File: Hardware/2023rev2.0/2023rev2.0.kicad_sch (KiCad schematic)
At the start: 94 parts

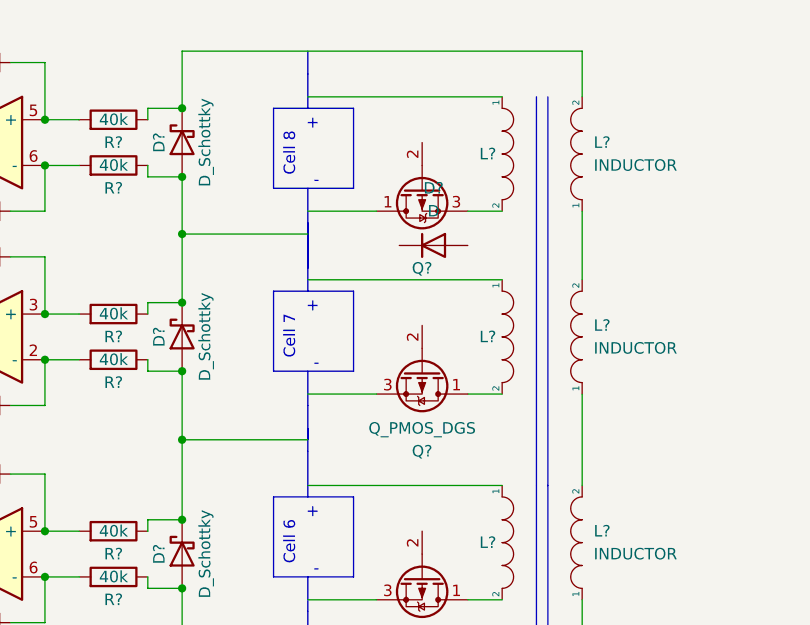
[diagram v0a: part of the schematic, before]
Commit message: Figuring out diode on secondary coils
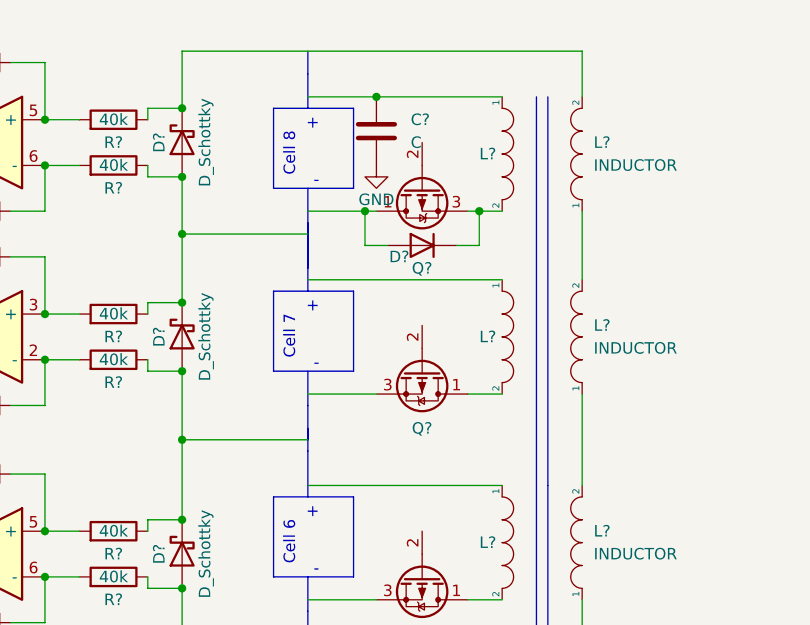
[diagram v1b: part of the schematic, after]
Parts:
- added C?: C, symbol Device:C
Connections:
- net GND: now also C?.2
- net at L?.1: now also C?.1
- net at L?.2, Q?.3 (S): now also D?.1 (K)
- net at Q?.1 (D): now also D?.2 (A)
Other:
- moved on the sheet: D?
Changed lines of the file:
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@@
   (junction (at 90.17 38.1) (diameter 0) (color 0 0 0 0)
   )
+  (junction (at 140.97 45.72) (diameter 0) (color 0 0 0 0)
+  )
   (junction (at 387.35 294.64) (diameter 0) (color 0 0 0 0)
   )
@@
   (junction (at 120.65 48.26) (diameter 0) (color 0 0 0 0)
   )
+  (junction (at 142.24 33.02) (diameter 0) (color 0 0 0 0)
+  )
   (junction (at 120.65 41.91) (diameter 0) (color 0 0 0 0)
   )
@@
   (junction (at 90.17 173.99) (diameter 0) (color 0 0 0 0)
   )
+  (junction (at 153.67 45.72) (diameter 0) (color 0 0 0 0)
+  )
   (junction (at 105.41 171.45) (diameter 0) (color 0 0 0 0)
   )
@@
     (stroke (width 0) (type default) (color 0 0 0 0))
   )
+  (wire (pts (xy 142.24 33.02) (xy 156.21 33.02))
+    (stroke (width 0) (type default) (color 0 0 0 0))
+  )
   (wire (pts (xy 386.08 294.64) (xy 387.35 294.64))
     (stroke (width 0) (type default) (color 0 0 0 0))
@@
     (stroke (width 0) (type default) (color 0 0 0 0))
   )
+  (wire (pts (xy 153.67 49.53) (xy 153.67 45.72))
+    (stroke (width 0) (type default) (color 0 0 0 0))
+  )
   (wire (pts (xy 327.66 283.21) (xy 292.1 283.21))
     (stroke (width 0) (type default) (color 0 0 0 0))
@@
     (stroke (width 0) (type default) (color 0 0 0 0))
   )
+  (wire (pts (xy 140.97 45.72) (xy 142.24 45.72))
+    (stroke (width 0) (type default) (color 0 0 0 0))
+  )
   (wire (pts (xy 87.63 186.69) (xy 93.98 186.69))
     (stroke (width 0) (type default) (color 0 0 0 0))
@@
     (stroke (width 0) (type default) (color 0 0 0 0))
   )
-  (wire (pts (xy 134.62 33.02) (xy 156.21 33.02))
+  (wire (pts (xy 134.62 33.02) (xy 142.24 33.02))
     (stroke (width 0) (type default) (color 0 0 0 0))
   )
@@
     (stroke (width 0) (type default) (color 0 0 0 0))
   )
+  (wire (pts (xy 151.13 49.53) (xy 153.67 49.53))
+    (stroke (width 0) (type default) (color 0 0 0 0))
+  )
   (wire (pts (xy 116.84 87.63) (xy 120.65 87.63))
     (stroke (width 0) (type default) (color 0 0 0 0))
   )
-  (wire (pts (xy 134.62 45.72) (xy 142.24 45.72))
+  (wire (pts (xy 134.62 45.72) (xy 140.97 45.72))
     (stroke (width 0) (type default) (color 0 0 0 0))
   )
@@
     (stroke (width 0) (type default) (color 0 0 0 0))
   )
+  (wire (pts (xy 143.51 49.53) (xy 140.97 49.53))
+    (stroke (width 0) (type default) (color 0 0 0 0))
+  )
   (wire (pts (xy 87.63 165.1) (xy 93.98 165.1))
     (stroke (width 0) (type default) (color 0 0 0 0))
@@
     (stroke (width 0) (type default) (color 0 0 0 0))
   )
+  (wire (pts (xy 153.67 45.72) (xy 156.21 45.72))
+    (stroke (width 0) (type default) (color 0 0 0 0))
+  )
+  (wire (pts (xy 140.97 49.53) (xy 140.97 45.72))
+    (stroke (width 0) (type default) (color 0 0 0 0))
+  )
   (wire (pts (xy 316.23 264.16) (xy 322.58 264.16))
     (stroke (width 0) (type default) (color 0 0 0 0))
@@
     (stroke (width 0) (type default) (color 0 0 0 0))
   )
-  (wire (pts (xy 152.4 45.72) (xy 156.21 45.72))
+  (wire (pts (xy 152.4 45.72) (xy 153.67 45.72))
     (stroke (width 0) (type default) (color 0 0 0 0))
   )
@@
     (pin "2")
   )
+  (symbol (lib_id "power:GND") (at 142.24 40.64 0) (unit 1)
+    (in_bom yes) (on_board yes)
+    (property "Reference" "#PWR?" (id 0) (at 142.24 46.99 0)
+      (effects (font (size 1.27 1.27)) hide)
+    )
+    (property "Value" "GND" (id 1) (at 142.24 44.45 0))
+    (property "Footprint" "" (id 2) (at 142.24 40.64 0)
+      (effects (font (size 1.27 1.27)) hide)
+    )
+    (property "Datasheet" "" (id 3) (at 142.24 40.64 0)
+      (effects (font (size 1.27 1.27)) hide)
+    )
+    (pin "1")
+  )
   (symbol (lib_id "power:GND") (at 87.63 139.7 90) (mirror x) (unit 1)
     (in_bom yes) (on_board yes) (fields_autoplaced)
@@
   (symbol (lib_id "Device:Q_PMOS_DGS") (at 147.32 63.5 270) (unit 1)
     (in_bom yes) (on_board yes)
-    (property "Reference" "Q?" (id 0) (at 147.32 72.39 90))
-    (property "Value" "Q_PMOS_DGS" (id 1) (at 147.32 69.85 90))
+    (property "Reference" "Q?" (id 0) (at 147.32 69.85 90))
+    (property "Value" "Q_PMOS_DGS" (id 1) (at 147.32 69.85 90)
+      (effects (font (size 1.27 1.27)) hide)
+    )
     (property "Footprint" "" (id 2) (at 149.86 68.58 0)
       (effects (font (size 1.27 1.27)) hide)
@@
     (pin "2")
   )
-  (symbol (lib_id "Device:D") (at 148.59 49.53 0) (unit 1)
-    (in_bom yes) (on_board yes) (fields_autoplaced)
-    (property "Reference" "D?" (id 0) (at 148.59 43.18 0))
-    (property "Value" "D" (id 1) (at 148.59 45.72 0))
-    (property "Footprint" "" (id 2) (at 148.59 49.53 0)
+  (symbol (lib_id "Device:D") (at 147.32 49.53 0) (mirror y) (unit 1)
+    (in_bom yes) (on_board yes)
+    (property "Reference" "D?" (id 0) (at 144.78 50.8 0))
+    (property "Value" "D" (id 1) (at 144.78 50.8 0)
       (effects (font (size 1.27 1.27)) hide)
     )
-    (property "Datasheet" "~" (id 3) (at 148.59 49.53 0)
+    (property "Footprint" "" (id 2) (at 147.32 49.53 0)
+      (effects (font (size 1.27 1.27)) hide)
+    )
+    (property "Datasheet" "~" (id 3) (at 147.32 49.53 0)
       (effects (font (size 1.27 1.27)) hide)
     )
@@
     (pin "2")
   )
+  (symbol (lib_id "Device:C") (at 142.24 36.83 0) (unit 1)
+    (in_bom yes) (on_board yes) (fields_autoplaced)
+    (property "Reference" "C?" (id 0) (at 146.05 35.5599 0)
+      (effects (font (size 1.27 1.27)) (justify left))
+    )
+    (property "Value" "C" (id 1) (at 146.05 38.0999 0)
+      (effects (font (size 1.27 1.27)) (justify left))
+    )
+    (property "Footprint" "" (id 2) (at 143.2052 40.64 0)
+      (effects (font (size 1.27 1.27)) hide)
+    )
+    (property "Datasheet" "~" (id 3) (at 142.24 36.83 0)
+      (effects (font (size 1.27 1.27)) hide)
+    )
+    (pin "1")
+    (pin "2")
+  )
   (symbol (lib_id "Device:Q_NMOS_DGS") (at 327.66 266.7 90) (unit 1)
     (in_bom yes) (on_board yes)
@@
       (reference "#PWR?") (unit 1) (value "GND") (footprint "")
     )
+    (path "/50afe7f4-8e1a-4d97-a4b7-7a2a9883e934"
+      (reference "#PWR?") (unit 1) (value "GND") (footprint "")
+    )
     (path "/5390dd54-0590-4ac8-afa3-1015cac016d4"
       (reference "#PWR?") (unit 1) (value "GND") (footprint "")
@@
       (reference "BZ?") (unit 1) (value "Buzzer") (footprint "MRDT_Devices:BUZZER_SMI_1324_TW_5V_2_R")
     )
+    (path "/c5e1abd5-6f6c-4b4a-9510-ae4bea6eeae4"
+      (reference "C?") (unit 1) (value "C") (footprint "")
+    )
     (path "/05cfdbda-932e-4ba4-b37b-c109de5f19df"

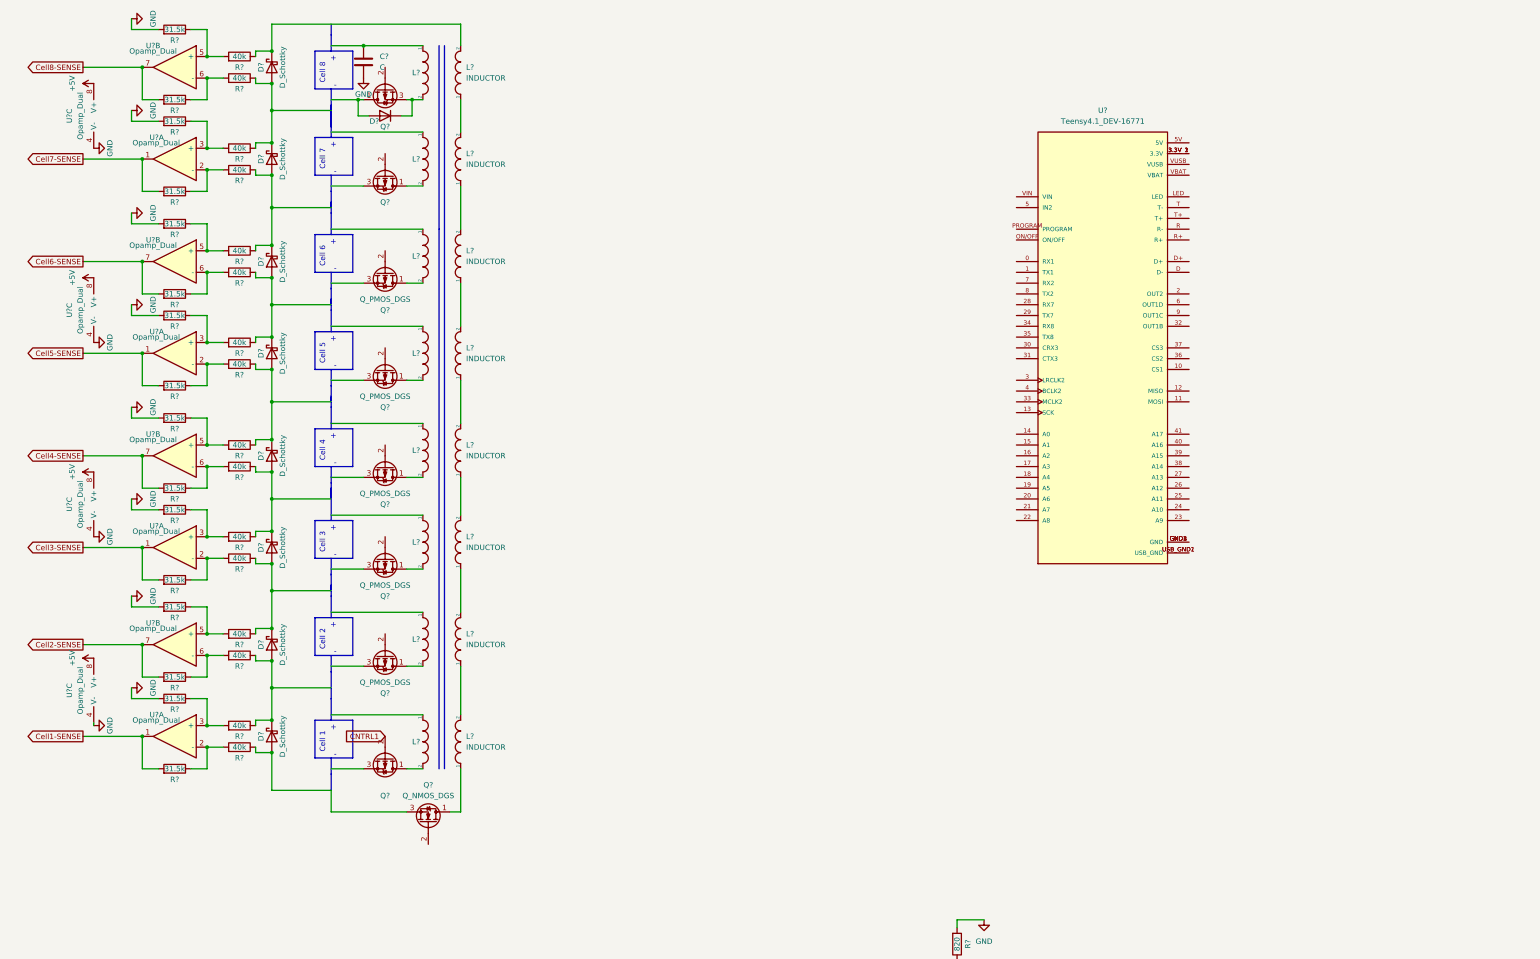
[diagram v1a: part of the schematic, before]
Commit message: New board schematic
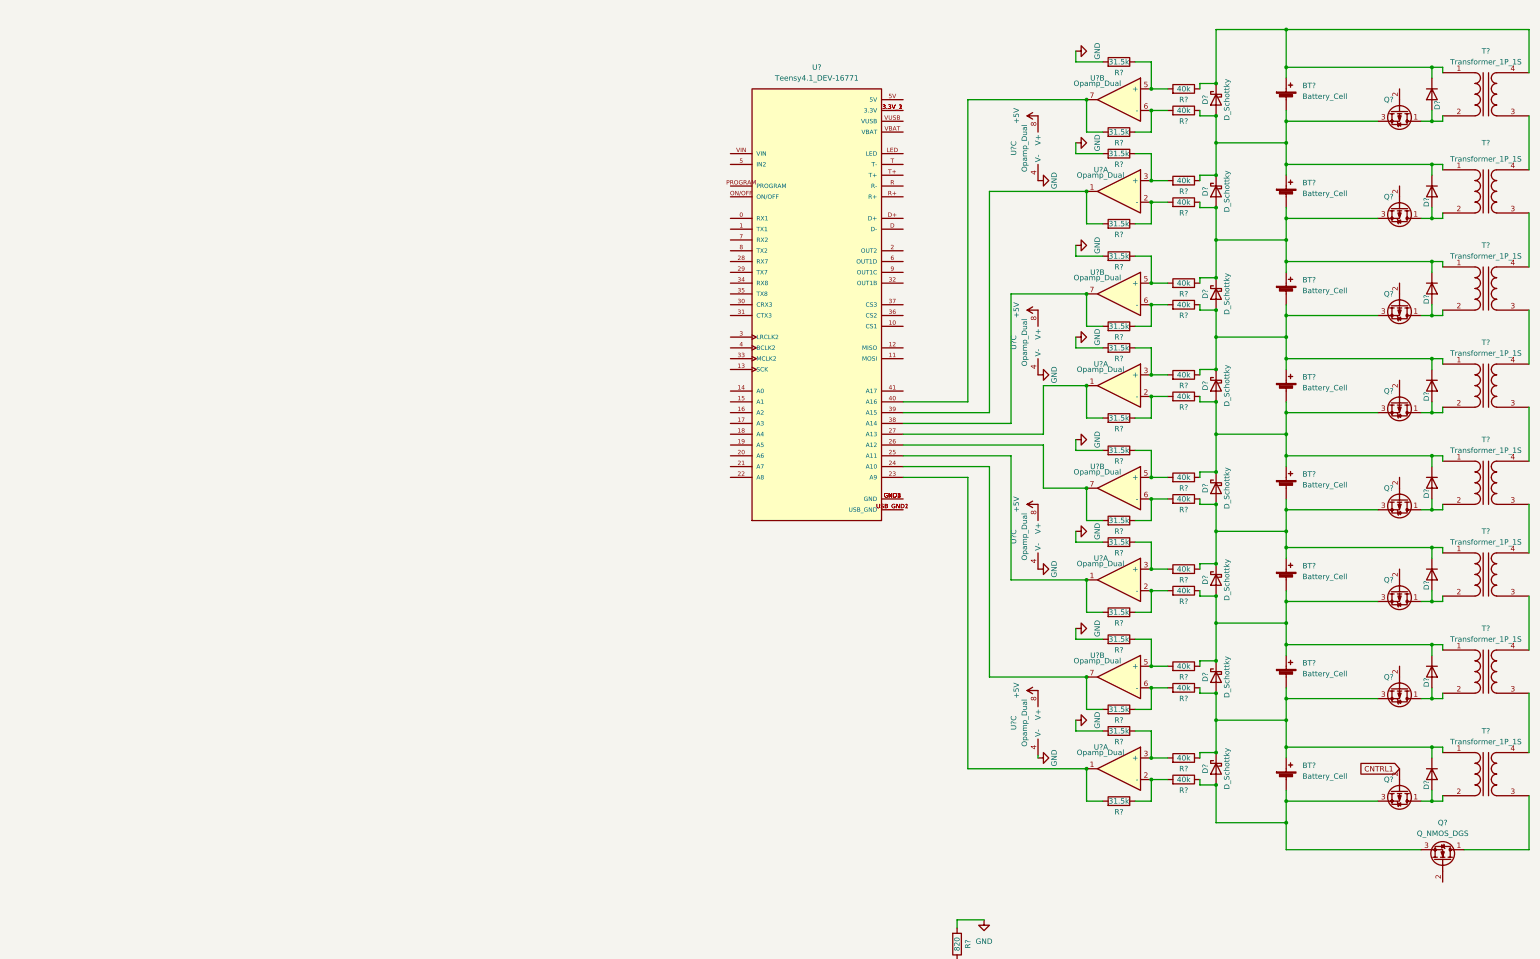
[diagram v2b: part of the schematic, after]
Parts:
- removed C?: C, symbol Device:C
- removed L? (x16): INDUCTOR, symbol pspice:INDUCTOR
- removed Q? (x7): Q_PMOS_DGS, symbol Device:Q_PMOS_DGS
- added BT? (x8): Battery_Cell, symbol Device:Battery_Cell
- added D? (x7): D, symbol Device:D
- added Q? (x7): Q_PMOS_DGS, symbol Device:Q_PMOS_DGS
- added T? (x8): Transformer_1P_1S, symbol Device:Transformer_1P_1S
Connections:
- net Cell1-SENSE is gone; now on an unnamed net: R?.2, U?.1
- net Cell2-SENSE is gone; now on an unnamed net: R?.2, U?.7
- net Cell3-SENSE is gone; now on an unnamed net: R?.2, U?.1
- net Cell4-SENSE is gone; now on an unnamed net: R?.2, U?.7
- net Cell5-SENSE is gone; now on an unnamed net: R?.2, U?.1
- net Cell6-SENSE is gone; now on an unnamed net: R?.2, U?.7
- net Cell7-SENSE is gone; now on an unnamed net: R?.2, U?.1
- net Cell8-SENSE is gone; now on an unnamed net: R?.2, U?.7
- net CNTRL1: now also Q?.2 (G)
- net at D?.1 (K), D?.2 (A), R?.1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: now also BT?.1 (+), BT?.2 (-), D?.1 (K), Q?.3 (S), T?.1 (AA) (x6)
- net at D?.1 (K), R?.1: now also D?.1 (K), BT?.1 (+), T?.1 (AA), T?.4 (SB)
- net at D?.1 (K), D?.2 (A), R?.1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: now also Q?.3 (S), BT?.1 (+), BT?.2 (-), D?.1 (K), T?.1 (AA)
- net at Q?.1 (D): now also T?.3 (SA)
- net at D?.2 (A), Q?.3 (S), R?.1: now also BT?.2 (-), Q?.3 (S)
- net at D?.2 (A), Q?.1 (D): now also T?.2 (AB)
- new net: T?.3 (SA), T?.4 (SB) (x7)
- new net: D?.2 (A), Q?.1 (D), T?.2 (AB) (x7)
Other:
- note removed: "+"
- note removed: "-"
- note removed: "Cell 1"
- note removed: "Cell 2"
- note removed: "Cell 3"
- note removed: "Cell 4"
- note removed: "Cell 5"
- note removed: "Cell 6"
- note removed: "Cell 7"
- note removed: "Cell 8"
- moved on the sheet: D?, Q?, R?, U?, U?A, U?B, U?C

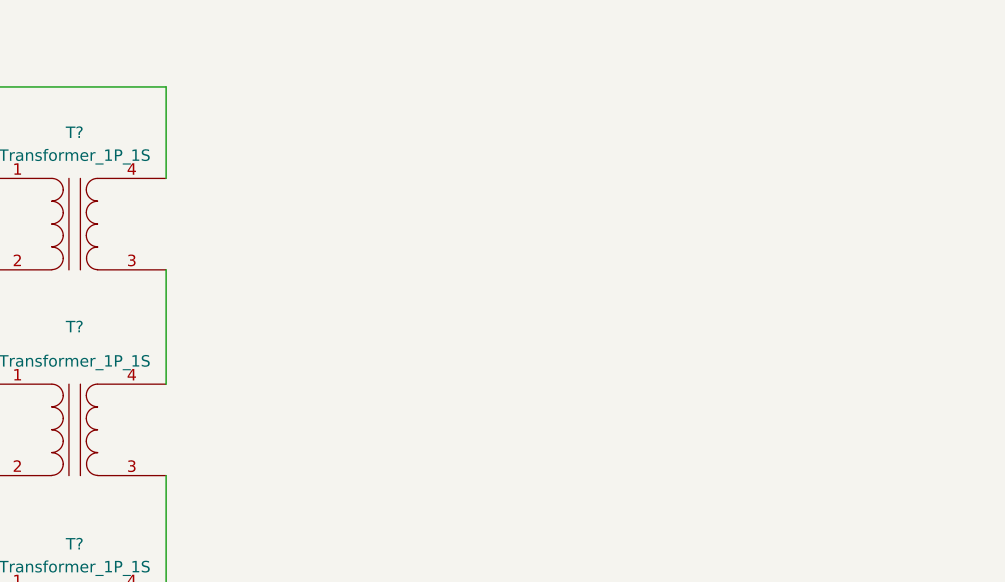
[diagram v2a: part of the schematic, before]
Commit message: Adding Current Shunt
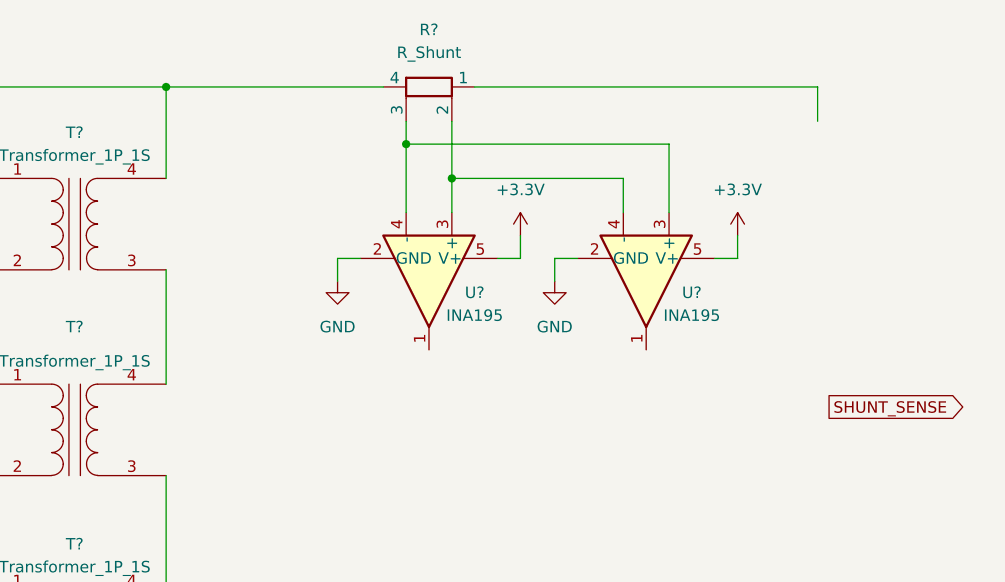
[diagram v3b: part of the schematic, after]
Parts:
- added R?: R_Shunt, symbol Device:R_Shunt
- added U? (x2): INA195, Package_TO_SOT_SMD:SOT-23-5, symbol Amplifier_Current:INA195
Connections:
- net +3.3V: now also U?.5 (V+), U?.5 (V+)
- net GND: now also U?.2 (GND), U?.2 (GND)
- net at BT?.1 (+), D?.1 (K), D?.1 (K)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: now also R?.4
- new net: R?.2, U?.3 (+), U?.4 (-)
- new net: R?.3, U?.3 (+), U?.4 (-)
